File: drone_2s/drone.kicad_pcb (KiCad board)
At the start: 2 copper layers, 50.8 x 50.8 mm, 45 parts, among them J1 Conn_01x06, J2 Conn_01x02, J3 Conn_01x02, J4 Conn_01x02, J5 Conn_01x02, J6 Conn_01x02, Q1 Si2319CDS, Q2 Si2319CDS, Q3 Si2319CDS, Q4 Si2319CDS, SW1 SW_Push_Open, SW2 SW_Push_Open, U1 ESP32-WROOM-32, U2 MPU-6050, U3 DWM1000, U4 BMP280, U5 LM1117MP-3.3

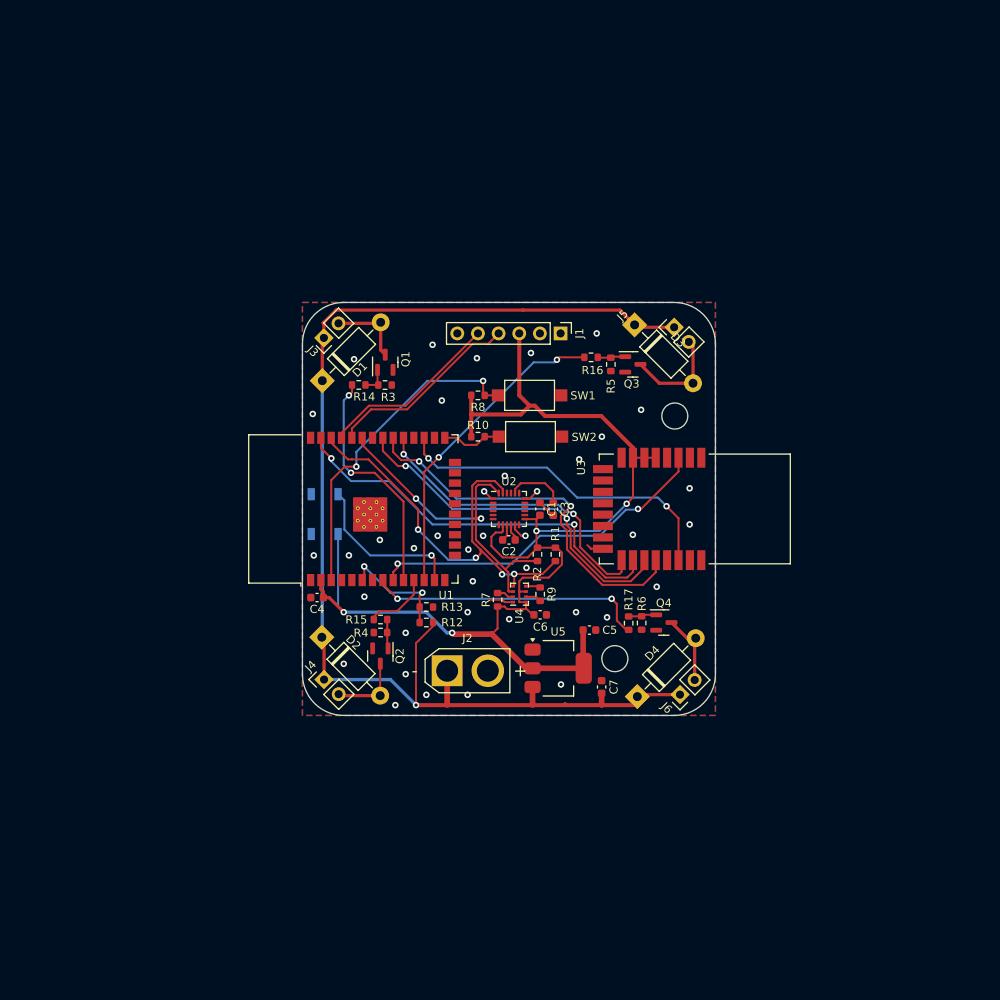
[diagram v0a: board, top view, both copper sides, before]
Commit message: motors mounted on pcb + usb program
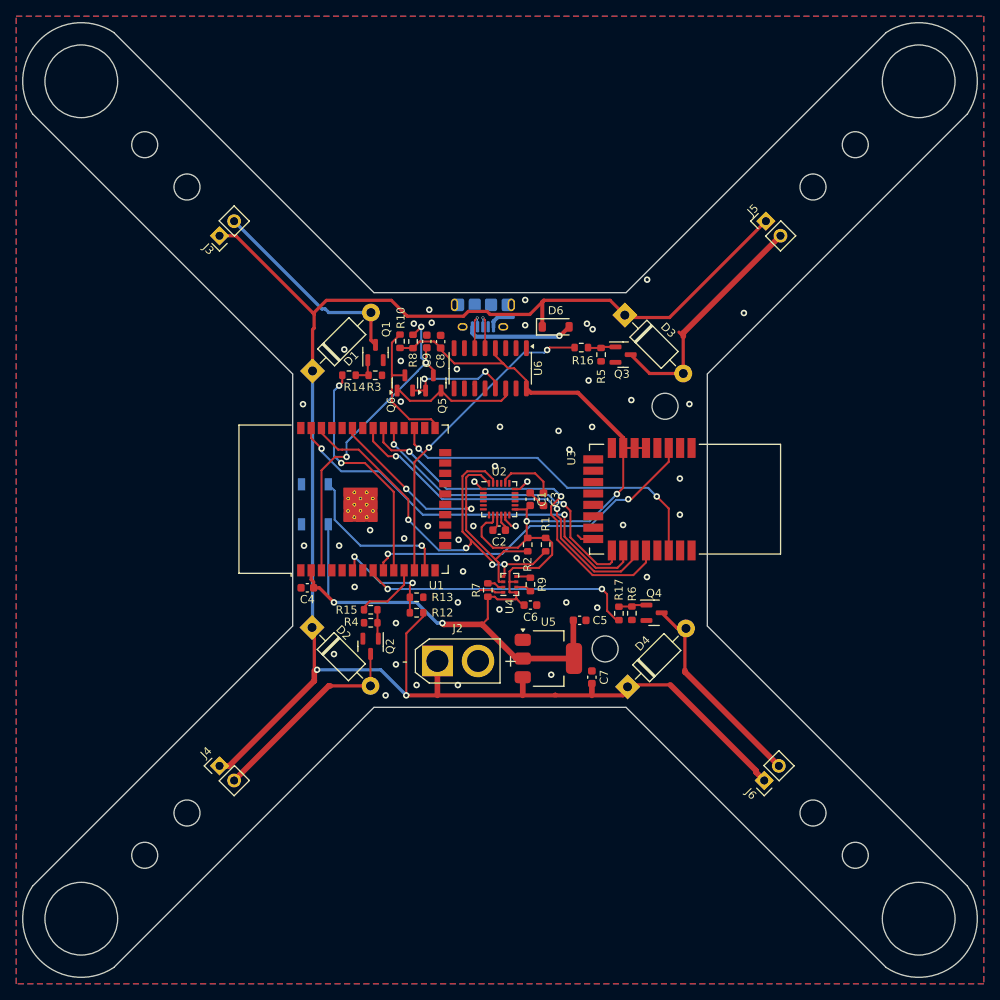
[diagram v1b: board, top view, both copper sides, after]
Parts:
- removed J1: Conn_01x06, Connector_PinHeader_2.54mm:PinHeader_1x06_P2.54mm_Vertical
- removed SW1, SW2: SW_Push_Open, Button_Switch_SMD:SW_SPST_CK_RS282G05A3
- added C8: C, Capacitor_SMD:C_0603_1608Metric, F.Cu at (93.2, 81.0)
- added C9: C, Capacitor_SMD:C_0603_1608Metric, F.Cu at (91.5, 81.0)
- added D6: 1N4148W, Diode_SMD:D_SOD-123, F.Cu at (107.3, 79.2)
- added J7: USB_B_Micro, Connector_USB:USB_Micro-B_Amphenol_10118194_Horizontal, B.Cu at (98.4, 77.8)
- added Q5: BSS138, Package_TO_SOT_SMD:SOT-23, F.Cu at (92.3, 86.1)
- added Q6: BSS138, Package_TO_SOT_SMD:SOT-23, F.Cu at (88.8, 86.1)
- added U6: CH340C, Package_SO:SOIC-16_3.9x9.9mm_P1.27mm, F.Cu at (99.3, 84.3)
- moved J3 18.0 mm to (66.0, 68.0)
- moved J5 17.3 mm to (133.2, 66.2)
- moved J4 16.7 mm to (66.0, 133.2)
- moved R10 15.2 mm to (88.2, 81.0), turned to 90 degrees
- moved J6 14.8 mm to (133.0, 135.0)
- moved R8 10.4 mm to (89.8, 81.0), turned to 90 degrees
- moved C3 1.70 mm to (105.8, 100.4)
- moved C4 1.70 mm to (76.8, 111.3)
- moved C5 1.70 mm to (110.3, 115.3)
- moved C6 1.70 mm to (104.2, 113.4)
- moved C7 1.70 mm to (111.8, 122.3)
- moved D1 1.70 mm to (77.4, 84.6)
- moved D2 1.70 mm to (77.4, 116.2)
- moved D4 1.70 mm to (116.2, 123.5)
- moved D5 1.70 mm to (77.7, 101.0)
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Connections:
- net Net-(SW1-B) renamed ESP32_EN
- net Net-(SW2-A) renamed ESP32_IO0
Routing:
- net BAT+: track 153.8 -> 226.3 mm, vias 1 -> 2
- net ESP_RX: track 24.0 -> 0.00 mm
- net ESP_TX: track 22.4 -> 0.58 mm
- net Net-(D3-A): track 12.7 -> 30.1 mm
- net Net-(D4-A): track 8.98 -> 25.5 mm
- net Net-(D1-A): track 10.2 -> 26.6 mm
- net Net-(D2-A): track 9.13 -> 25.5 mm
- net Net-(Q5-S): track 0.00 -> 16.1 mm
- net Net-(Q5-G): track 0.00 -> 13.6 mm, vias 0 -> 2
- net Net-(D6-A): track 0.00 -> 13.4 mm, vias 0 -> 1
- net ESP32_IO0: track 7.42 -> 17.3 mm
- net D-: track 0.00 -> 4.97 mm, vias 0 -> 1
- net D+: track 0.00 -> 4.93 mm, vias 0 -> 1
- net GND: track 17.0 -> 20.3 mm, vias 39 -> 50
- net VCC: track 152.9 -> 151.6 mm
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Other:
- board size 50.8 x 50.8 mm -> 117.4 x 117.4 mm

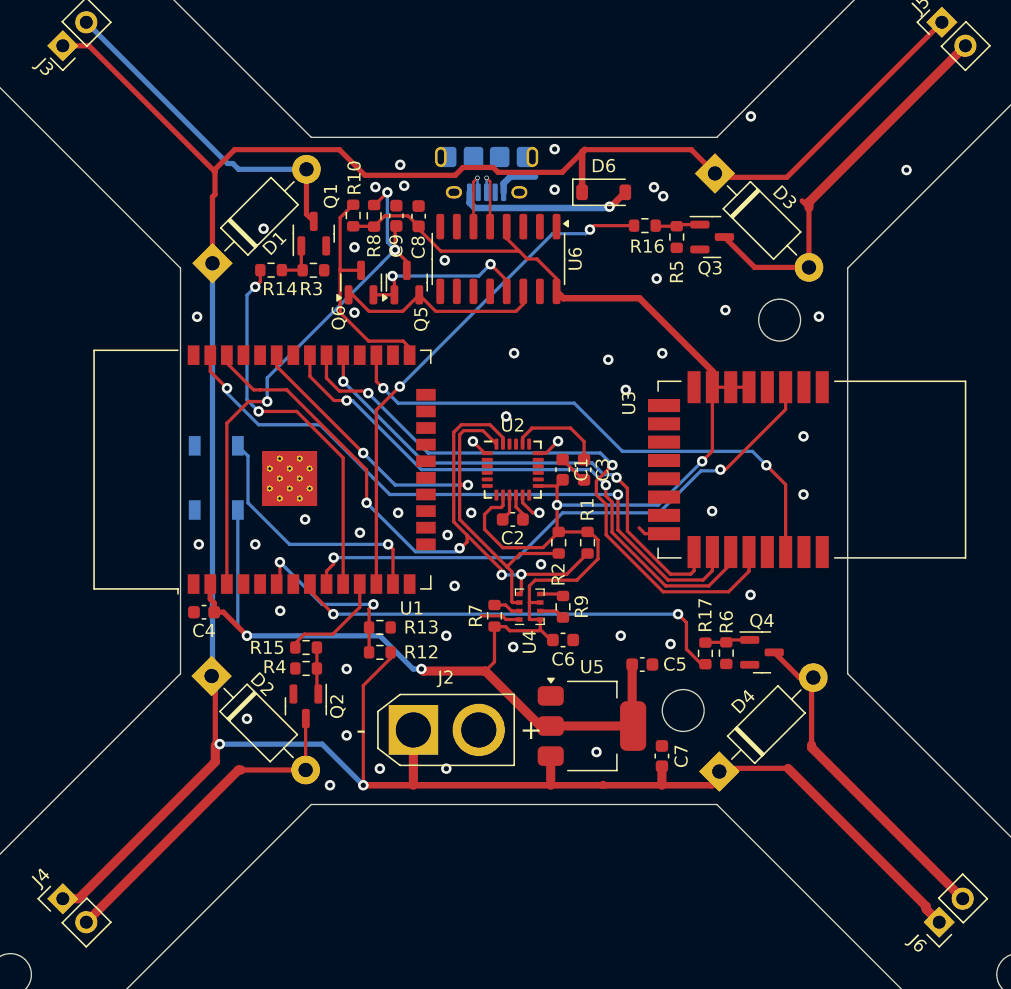
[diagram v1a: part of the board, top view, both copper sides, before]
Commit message: fix via size
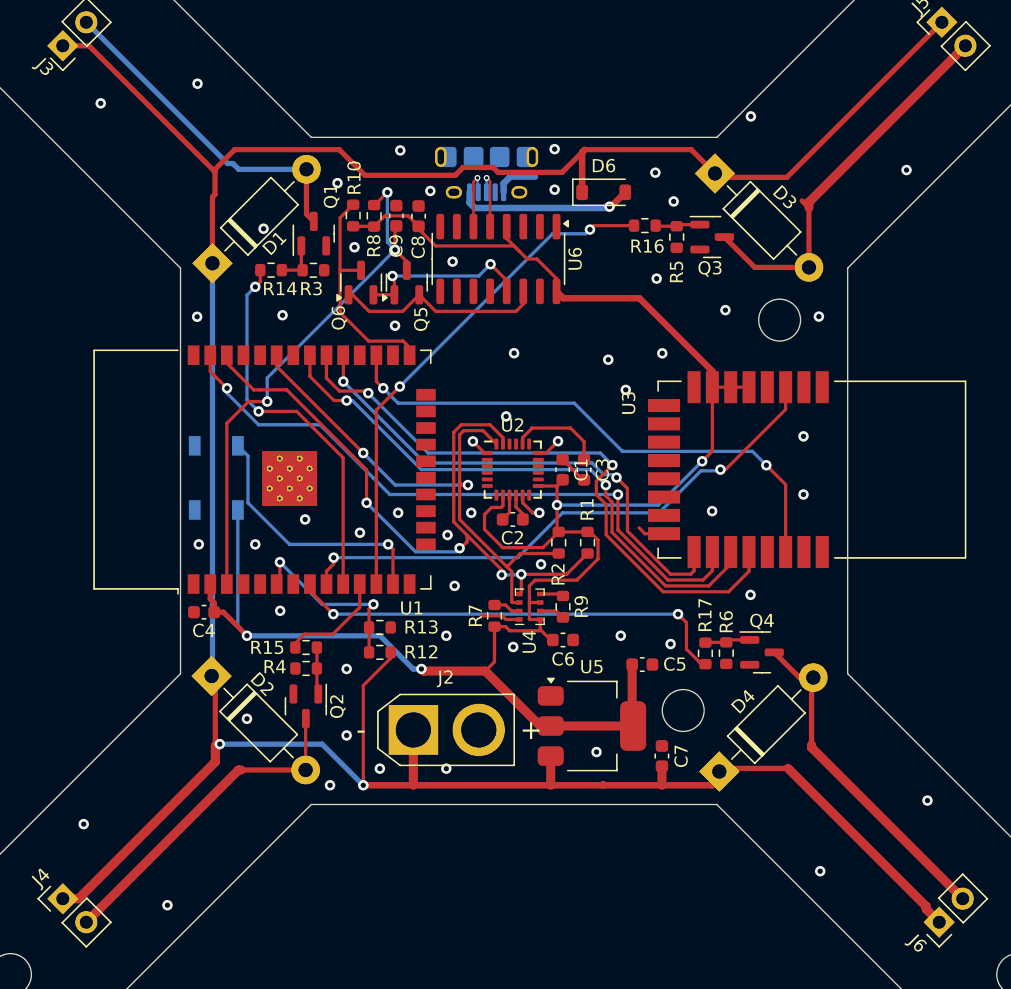
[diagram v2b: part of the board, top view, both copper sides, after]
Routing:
- net GND: vias 50 -> 57
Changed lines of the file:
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@@
 		(tags "SOD-123")
 		(property "Reference" "D6"
-			(at 0 -2 360)
+			(at 0 -2 0)
 			(layer "F.SilkS")
 			(effects
@@
 		)
 		(property "Value" "1N4148W"
-			(at 0 2.1 360)
+			(at 0 2.1 0)
 			(layer "F.Fab")
 			(effects
@@
 		)
 		(fp_text user "${REFERENCE}"
-			(at 0 -2 360)
+			(at 0 -2 0)
 			(layer "F.Fab")
 			(effects
@@
 	)
 	(via
+		(at 76.3 70.9)
+		(size 0.8)
+		(drill 0.4)
+		(layers "F.Cu" "B.Cu")
+		(free yes)
+		(net 34)
+	)
+	(via
 		(at 123.8 88.7)
 		(size 0.8)
@@
 	)
 	(via
+		(at 68.9 72.4)
+		(size 0.8)
+		(drill 0.4)
+		(layers "F.Cu" "B.Cu")
+		(free yes)
+		(net 34)
+	)
+	(via
 		(at 81.35 81.985)
 		(size 0.8)
@@
 	)
 	(via
-		(at 95.2 84.4)
+		(at 95.8 84.5)
 		(size 0.8)
 		(drill 0.4)
@@
 	)
 	(via
-		(at 88.3 88.4)
+		(at 67.6 127.5)
+		(size 0.8)
+		(drill 0.4)
+		(layers "F.Cu" "B.Cu")
+		(free yes)
+		(net 34)
+	)
+	(via
+		(at 74 133.7)
+		(size 0.8)
+		(drill 0.4)
+		(layers "F.Cu" "B.Cu")
+		(free yes)
+		(net 34)
+	)
+	(via
+		(at 91.4 89.4)
 		(size 0.8)
 		(drill 0.4)
@@
 	)
 	(via
-		(at 91.8 77.1)
+		(at 91.8 76)
 		(size 0.8)
 		(drill 0.4)
@@
 	)
 	(via
+		(at 82.8 88.6)
+		(size 0.8)
+		(drill 0.4)
+		(layers "F.Cu" "B.Cu")
+		(free yes)
+		(net 34)
+	)
+	(via
 		(at 102.432 103.702)
 		(size 0.8)
@@
 	)
 	(via
+		(at 132.1 125.7)
+		(size 0.8)
+		(drill 0.4)
+		(layers "F.Cu" "B.Cu")
+		(free yes)
+		(net 34)
+	)
+	(via
 		(at 111.83 91.51)
 		(size 0.8)
@@
 	)
 	(via
-		(at 111.195 78.81)
+		(at 111.3 77.7)
 		(size 0.8)
 		(drill 0.4)
@@
 	)
 	(via
+		(at 123.9 131.1)
+		(size 0.8)
+		(drill 0.4)
+		(layers "F.Cu" "B.Cu")
+		(free yes)
+		(net 34)
+	)
+	(via
 		(at 95.32 113.1)
 		(size 0.8)
@@
 	)
 	(via
-		(at 111.9 79.5)
+		(at 112.7 79.9)
 		(size 0.8)
 		(drill 0.4)
@@
 	)
 	(via
-		(at 92.1 78.7)
+		(at 94.1 79.1)
 		(size 0.8)
 		(drill 0.4)
@@
 	)
 	(via
-		(at 89.9 78.8)
+		(at 87 78.5)
 		(size 0.8)
 		(drill 0.4)
@@
 	)
 	(segment
-		(start 94.9 83.7)
-		(end 100.9 83.7)
-		(width 0.25)
-		(layer "F.Cu")
-		(net 38)
-	)
-	(segment
 		(start 99.935 82.735)
 		(end 99.935 81.825)
@@
 	)
 	(segment
-		(start 103.745 85.800001)
-		(end 102.244999 84.3)
+		(start 100.5 83.3)
+		(end 100.9 83.7)
 		(width 0.25)
 		(layer "F.Cu")
@@
 	)
 	(segment
-		(start 99.003 112.401)
-		(end 99.003 115.097)
+		(start 103.745 85.800001)
+		(end 102.244999 84.3)
 		(width 0.25)
 		(layer "F.Cu")
@@
 	)
 	(segment
-		(start 93.2 81.8)
-		(end 93.2 82)
+		(start 99.003 112.401)
+		(end 99.003 115.097)
 		(width 0.25)
 		(layer "F.Cu")
@@
 	)
 	(segment
-		(start 93.2 82)
-		(end 94.9 83.7)
-		(width 0.25)
-		(layer "F.Cu")
-		(net 38)
-	)
-	(segment
 		(start 98.241 103.829)
 		(end 98.241 104.972)
@@
 	)
 	(segment
+		(start 93.2 82)
+		(end 94.5 83.3)
+		(width 0.25)
+		(layer "F.Cu")
+		(net 38)
+	)
+	(segment
 		(start 103.3 120)
 		(end 102.5 120)
@@
 	)
 	(segment
+		(start 94.5 83.3)
+		(end 100.5 83.3)
+		(width 0.25)
+		(layer "F.Cu")
+		(net 38)
+	)
+	(segment
 		(start 101.67 109.29)
 		(end 101.67 110.56)
@@
 	)
 	(segment
+		(start 93.2 81.8)
+		(end 93.2 82)
+		(width 0.25)
+		(layer "F.Cu")
+		(net 38)
+	)
+	(segment
 		(start 104.27 87.3)
 		(end 103.745 86.775)
@@
 	(via
 		(at 97.7 78.1)
-		(size 0.35)
+		(size 0.45)
 		(drill 0.25)
 		(layers "F.Cu" "B.Cu")
@@
 	(via
 		(at 98.4 78.1)
-		(size 0.35)
+		(size 0.45)
 		(drill 0.25)
 		(layers "F.Cu" "B.Cu")

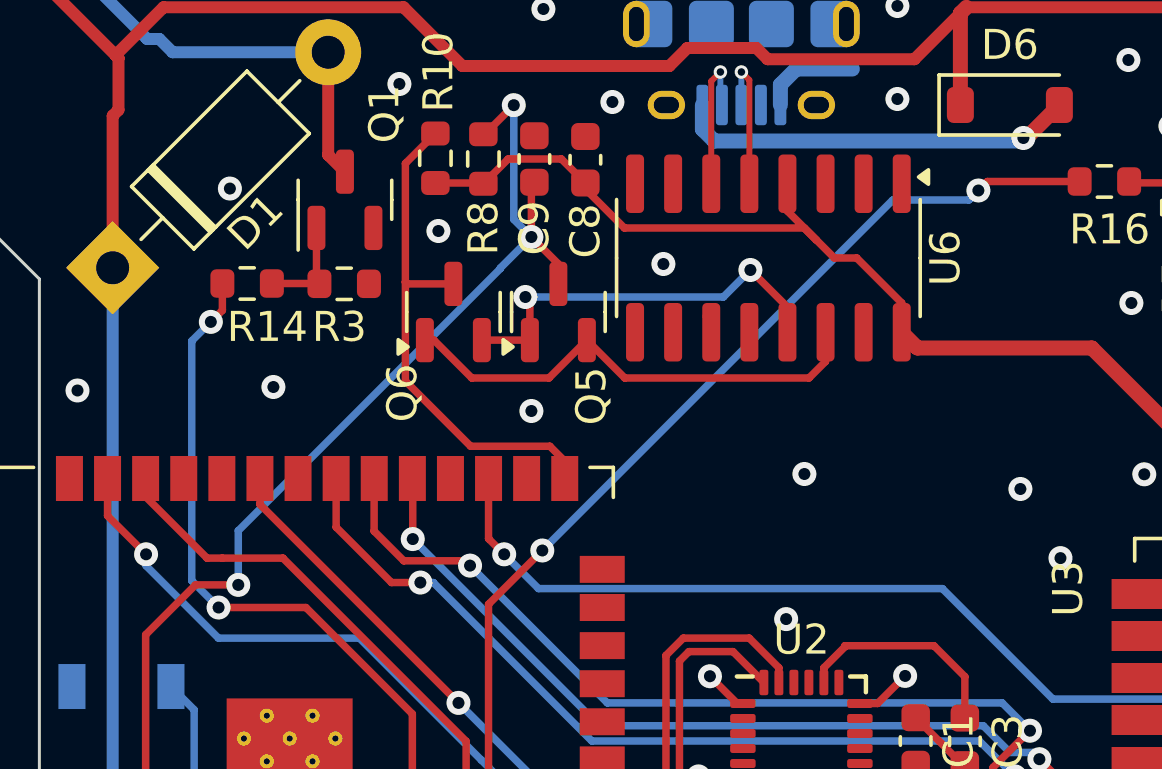
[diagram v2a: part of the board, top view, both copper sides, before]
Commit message: fix drone uart wiring
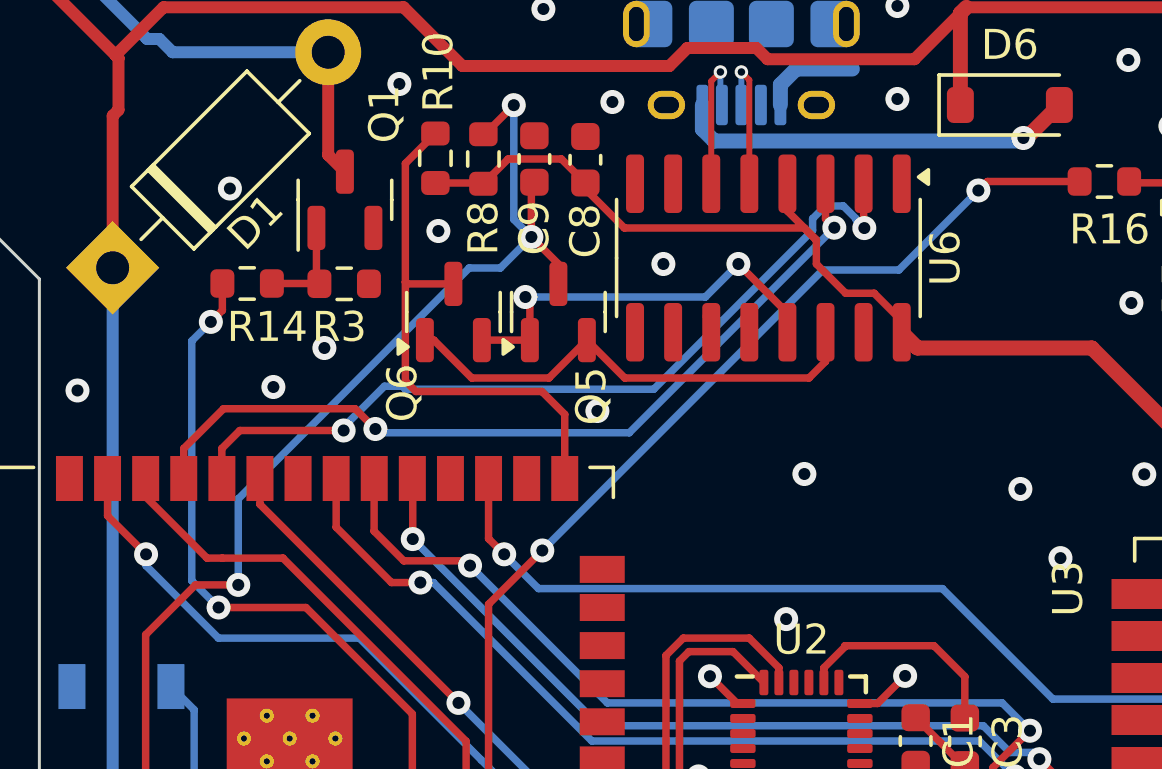
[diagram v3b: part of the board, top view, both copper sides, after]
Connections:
- U6 pad 2: TX-PROG -> ESP_RX
- U6 pad 3: RX-PROG -> ESP_TX
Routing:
- net ESP_RX: track 0.00 -> 28.0 mm, vias 0 -> 2
- net ESP_TX: track 0.58 -> 28.0 mm, vias 0 -> 2
- net ESP32_IO0: track 17.3 -> 18.2 mm
- net ESP32_EN: track 41.6 -> 42.2 mm
- net GND: vias 57 -> 58
